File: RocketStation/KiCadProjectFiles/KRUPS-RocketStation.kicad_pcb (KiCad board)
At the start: 4 copper layers, 85 x 56 mm, 46 parts, among them J1 XT30U-M, J2 USB_C_Receptacle_USB2.0_16P, J3 RPi5_Header, J4 B2P-VH-FB-B, J5 B2P-VH-FB-B, J6 B2P-VH-FB-B, U1 PKU5511ESI, U2 AZ1117-3.3, U3 BME280, U4 SP3232, U5 ESP32-S3-WROOM-2, U6 BNO086, U7 E22-900M33S

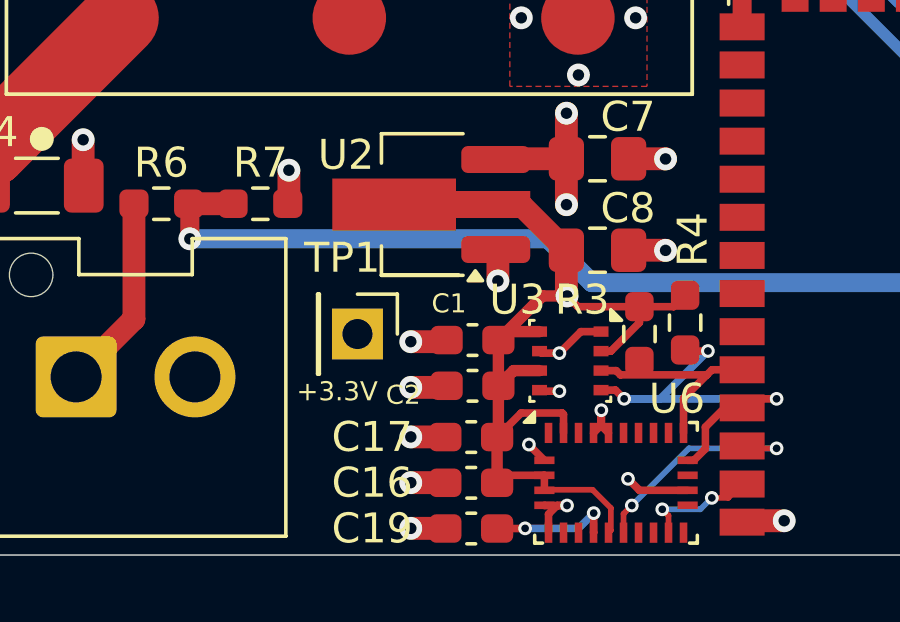
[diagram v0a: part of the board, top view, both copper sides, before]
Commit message: Small fixes for RocketStation v1
Modified RocketStation readme, fixed unconnected 3.3V test point, slightly changed async nets on schematic
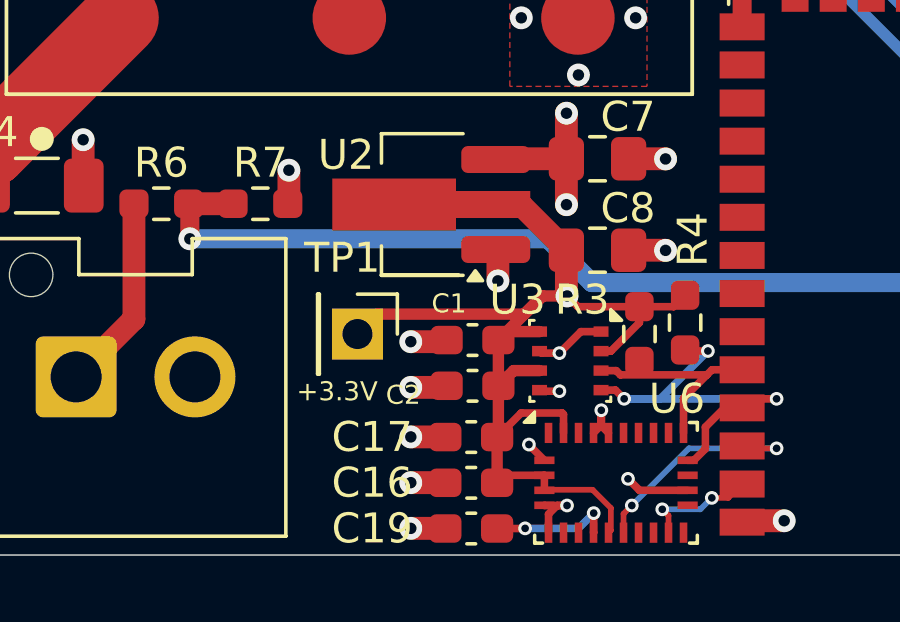
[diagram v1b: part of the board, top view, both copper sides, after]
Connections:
- J4 pad 2: /ASYNC_1 -> /ASYNC_2
- J6 pad 2: /ASYNC_2 -> /ASYNC_1
- U4 pad 14: /ASYNC_1 -> /ASYNC_2
- U4 pad 7: /ASYNC_2 -> /ASYNC_1
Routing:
- net /ASYNC_2: track 24.8 -> 7.64 mm
- net /ASYNC_1: track 7.64 -> 24.8 mm
- net +3V3: track 105.1 -> 111.8 mm
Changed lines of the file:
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@@
 			(layers "*.Cu" "*.Mask")
 			(remove_unused_layers no)
-			(net 52 "/ASYNC_2")
+			(net 51 "/ASYNC_1")
 			(pinfunction "Pin_2")
 			(pintype "passive")
@@
 			(layers "F.Cu" "F.Paste" "F.Mask")
 			(roundrect_rratio 0.25)
-			(net 52 "/ASYNC_2")
+			(net 51 "/ASYNC_1")
 			(pinfunction "T2OUT")
 			(pintype "output")
@@
 			(layers "F.Cu" "F.Paste" "F.Mask")
 			(roundrect_rratio 0.25)
-			(net 51 "/ASYNC_1")
+			(net 52 "/ASYNC_2")
 			(pinfunction "T1OUT")
 			(pintype "output")
@@
 			(layers "*.Cu" "*.Mask")
 			(remove_unused_layers no)
-			(net 51 "/ASYNC_1")
+			(net 52 "/ASYNC_2")
 			(pinfunction "Pin_2")
 			(pintype "passive")
@@
 	)
 	(segment
+		(start 84.5025 70.0695)
+		(end 83.838 70.734)
+		(width 0.381)
+		(layer "F.Cu")
+		(net 1)
+	)
+	(segment
+		(start 89.401 70.0695)
+		(end 84.5025 70.0695)
+		(width 0.381)
+		(layer "F.Cu")
+		(net 1)
+	)
+	(segment
 		(start 92.28375 76.533914)
 		(end 91.674986 75.92515)
@@
 	)
 	(segment
+		(start 90.0065 69.464)
+		(end 89.401 70.0695)
+		(width 0.381)
+		(layer "F.Cu")
+		(net 1)
+	)
+	(segment
 		(start 88.5355 72.459)
 		(end 89.0415 71.953)
@@
 	)
 	(segment
-		(start 99.291 41.4705)
-		(end 102.8045 44.984)
-		(width 0.381)
-		(layer "F.Cu")
-		(net 51)
-	)
-	(segment
-		(start 99.291 38.7985)
-		(end 99.291 41.4705)
-		(width 0.381)
-		(layer "F.Cu")
-		(net 51)
-	)
-	(segment
 		(start 95.014 30.729)
 		(end 95.776 29.967)
 		(width 0.381)
 		(layer "F.Cu")
-		(net 52)
+		(net 51)
 	)
 	(segment
@@
 		(width 0.381)
 		(layer "F.Cu")
-		(net 52)
+		(net 51)
 	)
 	(segment
@@
 		(width 0.381)
 		(layer "F.Cu")
-		(net 52)
+		(net 51)
 	)
 	(segment
@@
 		(width 0.381)
 		(layer "F.Cu")
-		(net 52)
+		(net 51)
 	)
 	(segment
@@
 		(width 0.381)
 		(layer "F.Cu")
-		(net 52)
+		(net 51)
 	)
 	(segment
@@
 		(width 0.381)
 		(layer "F.Cu")
-		(net 52)
+		(net 51)
 	)
 	(segment
@@
 		(width 0.381)
 		(layer "F.Cu")
-		(net 52)
+		(net 51)
 	)
 	(segment
@@
 		(width 0.381)
 		(layer "F.Cu")
-		(net 52)
+		(net 51)
 	)
 	(segment
@@
 		(width 0.381)
 		(layer "F.Cu")
-		(net 52)
+		(net 51)
 	)
 	(segment
@@
 		(width 0.381)
 		(layer "F.Cu")
+		(net 51)
+	)
+	(segment
+		(start 99.291 41.4705)
+		(end 102.8045 44.984)
+		(width 0.381)
+		(layer "F.Cu")
+		(net 52)
+	)
+	(segment
+		(start 99.291 38.7985)
+		(end 99.291 41.4705)
+		(width 0.381)
+		(layer "F.Cu")

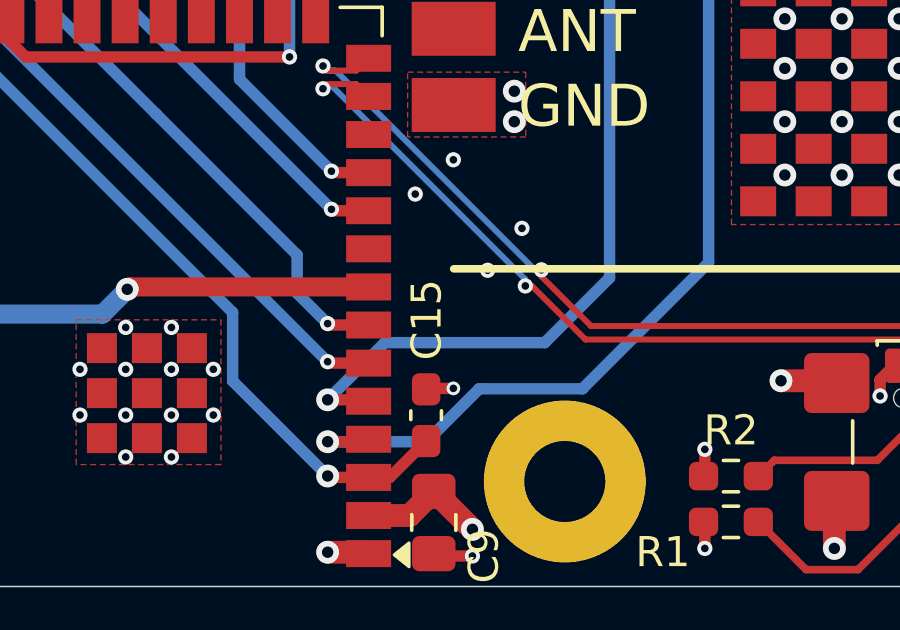
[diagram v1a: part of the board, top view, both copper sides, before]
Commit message: Added optional support for the LR62XE 1W radio
- Created a breakout/adapter board for the LR62XE 1W LoRa radio
- Modified the FemtoSat and RocketStation so that they'll be compatible with the adapter board
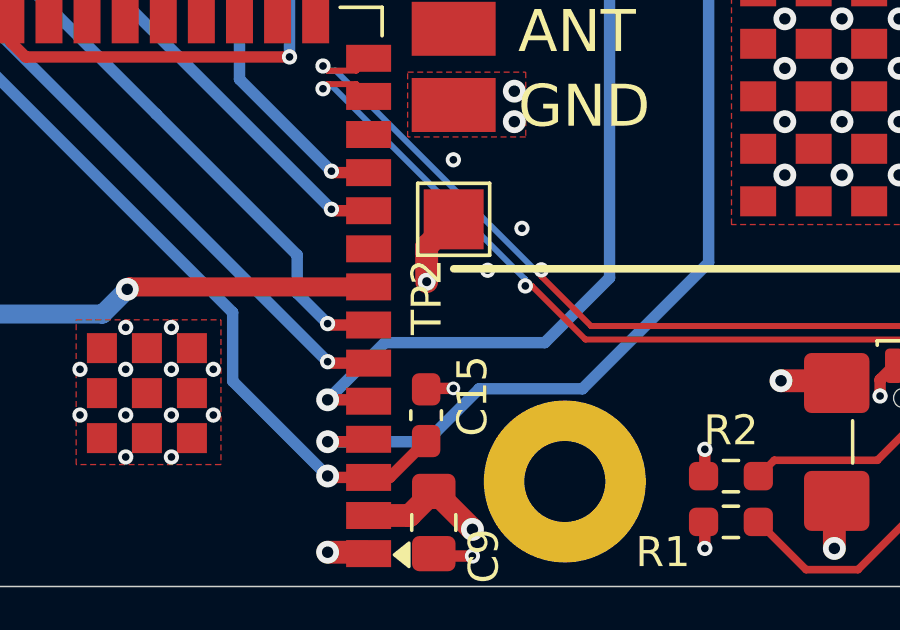
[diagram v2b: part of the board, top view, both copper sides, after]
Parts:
- added TP2: TestPoint, TestPoint:TestPoint_Pad_2.0x2.0mm, F.Cu at (117.0, 65.9)
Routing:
- net +3V3: track 111.8 -> 122.4 mm, vias 4 -> 5
- net GND: track 80.6 -> 80.1 mm, vias 117 -> 116
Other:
- board text added: "KRUPS BaseStation/RocketStation Rev: V2 Serial Number: 12-05-2024"
- board text removed: "KRUPS BaseStation/RocketStation Rev: V1 Serial Number: 11-17-2024"
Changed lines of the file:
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@@
 	(paper "A5")
 	(title_block
-		(date "2024-11-17")
-		(rev "V1")
+		(date "2024-12-05")
+		(rev "V2")
 	)
 	(layers
@@
 		)
 	)
+	(footprint "TestPoint:TestPoint_Pad_2.0x2.0mm"
+		(layer "F.Cu")
+		(at 116.995 65.86)
+		(descr "SMD rectangular pad as test Point, square 2.0mm side length")
+		(tags "test point SMD pad rectangle square")
+		(property "Reference" "TP2"
+			(at -0.899 2.588 90)
+			(layer "F.SilkS")
+			(effects
+				(font
+					(size 1 1)
+					(thickness 0.15)
+				)
+			)
+		)
+		(property "Value" "TestPoint"
+			(at 0 2.05 0)
+			(layer "F.Fab")
+			(effects
+				(font
+					(size 1 1)
+					(thickness 0.15)
+				)
+			)
+		)
+		(property "Footprint" "TestPoint:TestPoint_Pad_2.0x2.0mm"
+			(at 0 0 0)
+			(unlocked yes)
+			(layer "F.Fab")
+			(hide yes)
+			(effects
+				(font
+					(size 1.27 1.27)
+					(thickness 0.15)
+				)
+			)
+		)
+		(property "Datasheet" ""
+			(at 0 0 0)
+			(unlocked yes)
+			(layer "F.Fab")
+			(hide yes)
+			(effects
+				(font
+					(size 1.27 1.27)
+					(thickness 0.15)
+				)
+			)
+		)
+		(property "Description" "test point"
+			(at 0 0 0)
+			(unlocked yes)
+			(layer "F.Fab")
+			(hide yes)
+			(effects
+				(font
+					(size 1.27 1.27)
+					(thickness 0.15)
+				)
+			)
+		)
+		(property ki_fp_filters "Pin* Test*")
+		(sheetname "Root")
+		(sheetfile "KRUPS-RocketStation.kicad_sch")
+		(attr exclude_from_pos_files exclude_from_bom)
+		(fp_line
+			(start -1.2 -1.2)
+			(end 1.2 -1.2)
+			(stroke
+				(width 0.12)
+				(type solid)
+			)
+			(layer "F.SilkS")
+		)
+		(fp_line
+			(start -1.2 1.2)
+			(end -1.2 -1.2)
+			(stroke
+				(width 0.12)
+				(type solid)
+			)
+			(layer "F.SilkS")
+		)
+		(fp_line
+			(start 1.2 -1.2)
+			(end 1.2 1.2)
+			(stroke
+				(width 0.12)
+				(type solid)
+			)
+			(layer "F.SilkS")
+		)
+		(fp_line
+			(start 1.2 1.2)
+			(end -1.2 1.2)
+			(stroke
+				(width 0.12)
+				(type solid)
+			)
+			(layer "F.SilkS")
+		)
+		(fp_line
+			(start -1.5 -1.5)
+			(end -1.5 1.5)
+			(stroke
+				(width 0.05)
+				(type solid)
+			)
+			(layer "F.CrtYd")
+		)
+		(fp_line
+			(start -1.5 -1.5)
+			(end 1.5 -1.5)
+			(stroke
+				(width 0.05)
+				(type solid)
+			)
+			(layer "F.CrtYd")
+		)
+		(fp_line
+			(start 1.5 1.5)
+			(end -1.5 1.5)
+			(stroke
+				(width 0.05)
+				(type solid)
+			)
+			(layer "F.CrtYd")
+		)
+		(fp_line
+			(start 1.5 1.5)
+			(end 1.5 -1.5)
+			(stroke
+				(width 0.05)
+				(type solid)
+			)
+			(layer "F.CrtYd")
+		)
+		(fp_text user "${REFERENCE}"
+			(at 0 -2 0)
+			(layer "F.Fab")
+			(effects
+				(font
+					(size 1 1)
+					(thickness 0.15)
+				)
+			)
+		)
+		(pad "1" smd rect
+			(at 0 0)
+			(size 2 2)
+			(layers "F.Cu" "F.Mask")
+			(net 1 "+3V3")
+			(pinfunction "1")
+			(pintype "passive")
+		)
+	)
 	(footprint "KRUPS-RocketStation:JST_VH_B2P-VH-FB-B_1x02_P3.96mm_Vertical"
 		(layer "F.Cu")
@@
 		(tags "capacitor handsolder")
 		(property "Reference" "C15"
-			(at 3.18 0.018 90)
+			(at 0.64 1.542 90)
 			(layer "F.SilkS")
 			(effects
@@
 		)
 	)
-	(gr_text "KRUPS BaseStation/RocketStation\nRev: V1\nSerial Number:\n11-17-2024"
+	(gr_text "KRUPS BaseStation/RocketStation\nRev: V2\nSerial Number:\n12-05-2024"
 		(at 143.02 73.02 0)
 		(layer "B.SilkS")
@@
 		)
 		(height -12.644)
-		(gr_text "49.0000 mm"
+		(gr_text "1929.1339 mils"
 			(at 48.906 50.1 90)
 			(layer "Cmts.User")
@@
 		)
 		(height -11.718)
-		(gr_text "56.0000 mm"
+		(gr_text "2204.7244 mils"
 			(at 151.268 50.1 90)
 			(layer "Cmts.User")
@@
 		)
 		(height 1.94)
-		(gr_text "6.0000 mm"
+		(gr_text "236.2205 mils"
 			(at 118 83 90)
 			(layer "Cmts.User")
@@
 		)
 		(height -6.428)
-		(gr_text "85.0000 mm"
+		(gr_text "3346.4567 mils"
 			(at 101.7 18.022 0)
 			(layer "Cmts.User")
@@
 		)
 		(height 15.945999)
-		(gr_text "58.0000 mm"
+		(gr_text "2283.4646 mils"
 			(at 91.7 89.395999 0)
 			(layer "Cmts.User")
@@
 		)
 		(height 3.003999)
-		(gr_text "18.0000 mm"
+		(gr_text "708.6614 mils"
 			(at 105.41 86.347999 0)
 			(layer "Cmts.User")
@@
 	)
 	(segment
+		(start 116.096 67.94)
+		(end 116.096 66.759)
+		(width 0.762)
+		(layer "F.Cu")
+		(net 1)
+	)
+	(segment
 		(start 88.7425 75.442)
 		(end 88.4925 75.692)
@@
 	)
 	(segment
+		(start 116.096 66.759)
+		(end 116.995 65.86)
+		(width 0.762)
+		(layer "F.Cu")
+		(net 1)
+	)
+	(segment
 		(start 90.706 73.411)
 		(end 90.66 73.365)
@@
 	)
 	(via
+		(at 116.096 67.94)
+		(size 0.6)
+		(drill 0.3)
+		(layers "F.Cu" "B.Cu")
+		(net 1)
+	)
+	(via
 		(at 101.999 40)
 		(size 0.762)
@@
 	)
 	(segment
+		(start 115.588 75.941)
+		(end 117.366 75.941)
+		(width 0.762)
+		(layer "In2.Cu")
+		(net 1)
+	)
+	(segment
 		(start 96.919 40)
 		(end 101.999 40)
@@
 	)
 	(segment
+		(start 97.3 75.941)
+		(end 115.588 75.941)
+		(width 0.762)
+		(layer "In2.Cu")
+		(net 1)
+	)
+	(segment
 		(start 95.9355 40.9835)
 		(end 96.919 40)
@@
 	)
 	(segment
-		(start 97.3 75.941)
-		(end 117.366 75.941)
+		(start 115.588 75.941)
+		(end 116.096 75.433)
+		(width 0.762)
+		(layer "In2.Cu")
+		(net 1)
+	)
+	(segment
+		(start 116.096 75.433)
+		(end 116.096 67.94)
 		(width 0.762)
 		(layer "In2.Cu")
@@
 	)
 	(via
-		(at 115.715 65.019)
-		(size 0.508)
-		(drill 0.254)
-		(layers "F.Cu" "B.Cu")
-		(free yes)
-		(net 2)
-	)
-	(via
 		(at 138.956 59.939)
 		(size 0.762)
@@
 		(width 0.381)
 		(layer "In2.Cu")
-		(net 2)
-	)
-	(segment
-		(start 115.715 65.019)
-		(end 116.096 64.638)
-		(width 0.381)
-		(layer "In2.Cu")

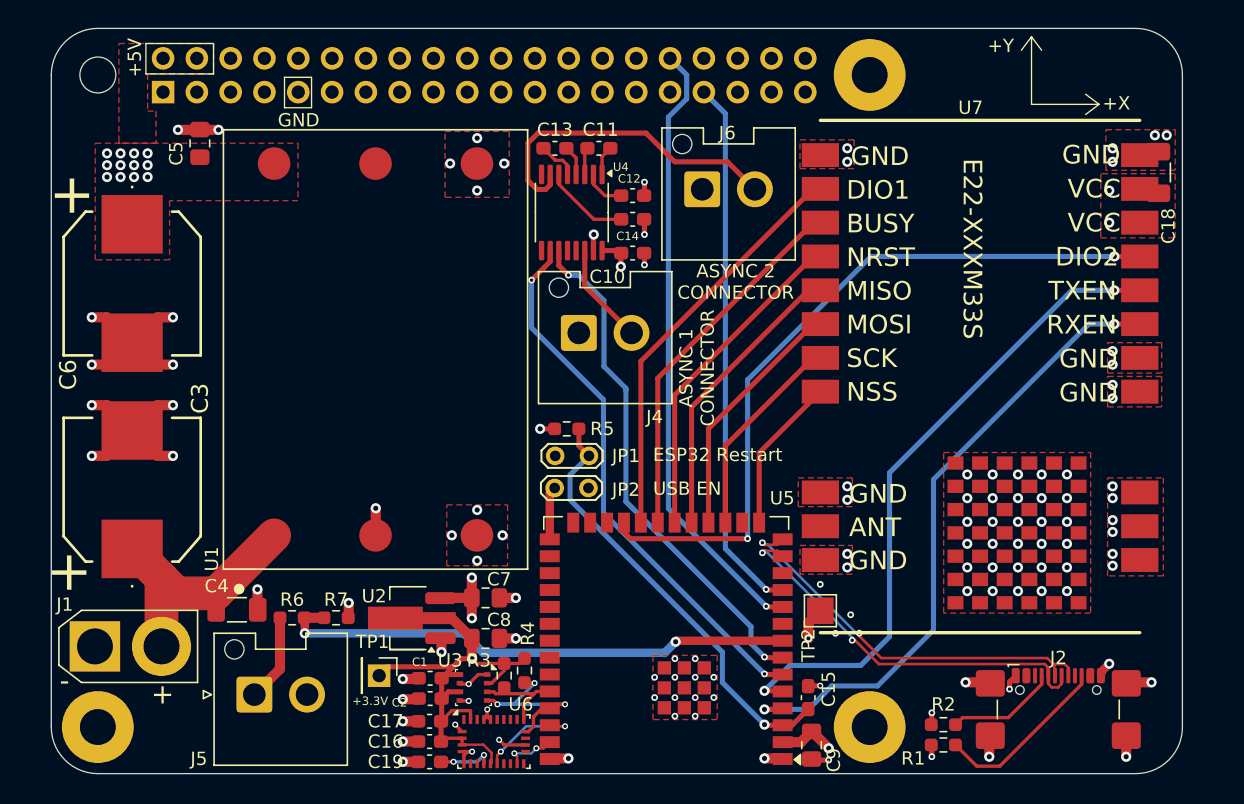
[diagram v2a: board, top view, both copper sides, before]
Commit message: Design Review Updates
Large number of design changes to both the FemtoSat (V5) and RocketStation (V3)

On both boards:
- Swapped the ESP32-S3-WROOM-2 modules to WROOM-1 modules due to supply issues
- Swapped power connectors to JST VH, data connectors to JST GH
- Added "Space Systems Lab, University of Kentucky, Lexington KY, USA, Earth" to the silkscreens
- Added test pads for IO pins, I2C bus, power
- Added LEDs connected to IO pins
- Changed power indication LEDs to a brighter LED
- Reformatted BOMs, they can now be generated by KiCad rather than being made by hand
- Updated documentation, 3D models

For Femtosat
- Removed 1 enclosure switch & MOSFET
- Moved a screw hole

and a bunch of other minor changes that I've forgotten
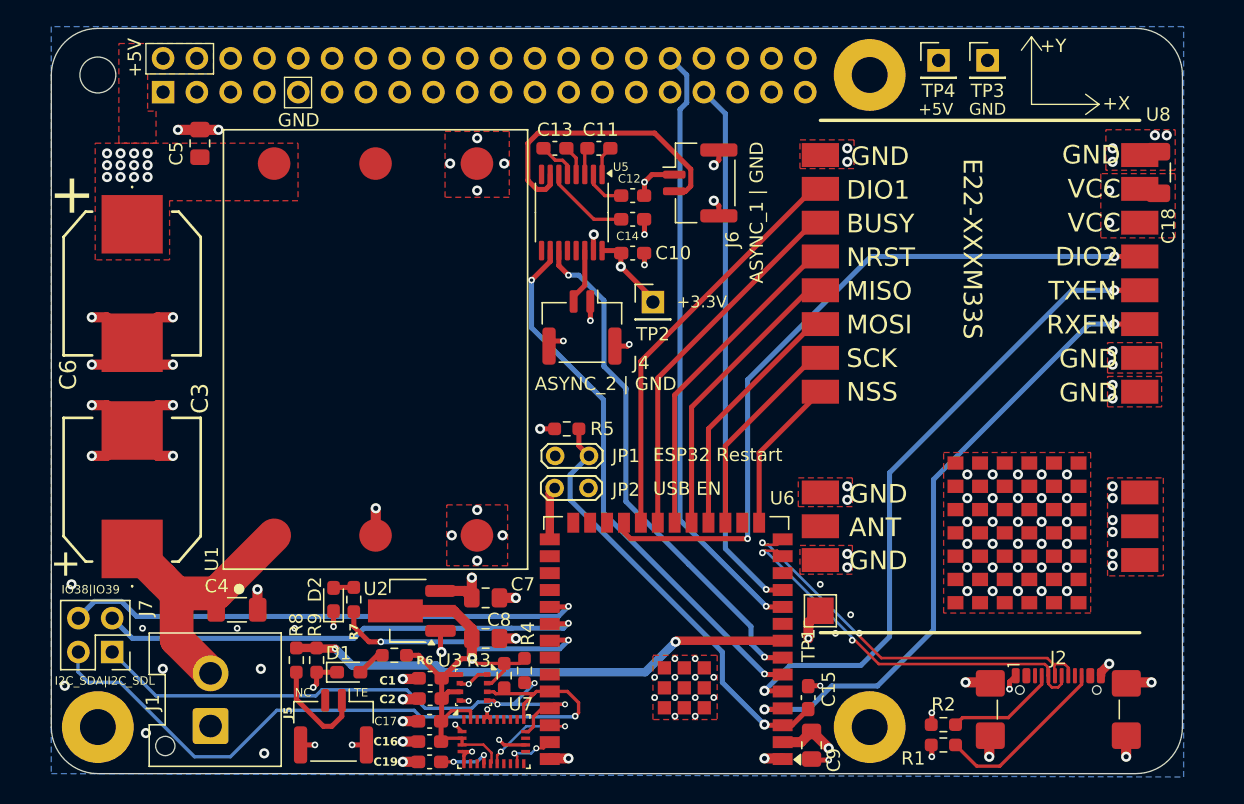
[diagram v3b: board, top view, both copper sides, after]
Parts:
- removed the TP1 at (83.8, 70.7)
- added D1: LED, Diode_SMD:D_0603_1608Metric_Pad1.05x0.95mm_HandSolder, F.Cu at (81.6, 70.5)
- added D2: LED, Diode_SMD:D_0603_1608Metric_Pad1.05x0.95mm_HandSolder, F.Cu at (80.4, 65.0)
- added J7: Conn_02x02, Connector_PinHeader_2.54mm:PinHeader_2x02_P2.54mm_Vertical, F.Cu at (63.8, 69.0)
- added R6: 68, Resistor_SMD:R_0603_1608Metric_Pad0.98x0.95mm_HandSolder, F.Cu at (85.0, 69.2)
- added R7: 68, Resistor_SMD:R_0603_1608Metric_Pad0.98x0.95mm_HandSolder, F.Cu at (81.9, 65.0)
- added TP2: TestPoint, Connector_PinHeader_2.54mm:PinHeader_1x01_P2.54mm_Vertical, F.Cu at (104.4, 42.7)
- added TP3: TestPoint, Connector_PinHeader_2.54mm:PinHeader_1x01_P2.54mm_Vertical, F.Cu at (129.6, 24.5)
- added TP4: TestPoint, Connector_PinHeader_2.54mm:PinHeader_1x01_P2.54mm_Vertical, F.Cu at (125.9, 24.5)
- J1: value XT30U-M -> B2P-VH-FB-B; footprint Connector_AMASS:AMASS_XT30U-M_1x02_P5.0mm_Vertical -> Connector_JST:JST_VH_B2P-VH-FB-B_1x02_P3.96mm_Vertical
- J4, J5, J6: value B2P-VH-FB-B -> BM02B-GHS-TBT; footprint KRUPS-RocketStation:JST_VH_B2P-VH-FB-B_1x02_P3.96mm_Vertical -> Connector_JST:JST_GH_BM02B-GHS-TBT_1x02-1MP_P1.25mm_Vertical
- moved J1 10.5 mm to (71.2, 74.5), turned to 90 degrees
- moved J5 6.41 mm to (80.4, 74.5), turned to 180 degrees
- moved R9 3.50 mm to (79.1, 69.6), turned to 90 degrees
- moved R8 3.19 mm to (77.6, 69.6), turned to -90 degrees
- moved U2 0.55 mm to (86.0, 65.9)
- moved J6 0.50 mm to (108.0, 33.7), turned to -90 degrees
- moved J4 0.47 mm to (99.1, 44.6), turned to 180 degrees
- renumbered R6 to R8, R7 to R9, TP2 to TP1, U4 to U5, U5 to U6, U6 to U7, U7 to U8
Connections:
- U6 pad 31: unconnected-(U5-IO38-Pad31) -> /IO38
- U6 pad 32: unconnected-(U5-MTCK/IO39-Pad32) -> /IO39
- U6 pad 33: unconnected-(U5-MTDO/IO40-Pad33) -> /IO40
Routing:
- net /I2C_SDA: track 7.09 -> 53.9 mm, vias 0 -> 1
- net /IO38: track 0.00 -> 39.6 mm, vias 0 -> 1
- net /IO39: track 0.00 -> 36.8 mm, vias 0 -> 1
- net /I2C_SCL: track 14.4 -> 45.8 mm
- net /IO40: track 0.00 -> 19.6 mm, vias 0 -> 2
- net GND: track 80.1 -> 93.8 mm, vias 116 -> 133
- net /ASYNC_2: track 7.64 -> 4.17 mm
- net /ASYNC_1: track 24.8 -> 22.0 mm
- net +5V: track 127.1 -> 129.2 mm, vias 16 -> 15
- net Net-(D1-A): track 0.00 -> 2.17 mm
- net Net-(J1-Pin_2): track 19.0 -> 20.9 mm
- net +3V3: track 122.4 -> 124.3 mm
- net Net-(D2-A): track 0.00 -> 1.54 mm
- net /TE_SENSE: track 39.6 -> 38.3 mm
- net Net-(J5-Pin_1): track 6.57 -> 7.80 mm
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- added copper zone on B.Cu, net GND
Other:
- board text added: "+"
- board text added: "+18V TO +75V"
- board text added: "-"
- board text added: "ASYNC_1 | GND"
- board text added: "ASYNC_2 | GND"
- board text added: "All mounting holes are M2.5 The height of the 40 pin GPIO connector can be adjusted during PCB assembly (the length of the connector's leads will be pretty long), so the height shown in the 3D model is not accurate"
- board text added: "I2C_SDA|I2C_SDL"
- board text added: "IO38|IO39"
- board text added: "NC"
- board text added: "Space Systems Lab, University of Kentucky, Lexington KY, USA, Earth KRUPS BaseStation/RocketStation Rev: V3 Serial Number: 12-27-2024"
- board text added: "TE"
- board text removed: "ASYNC 1 CONNECTOR"
- board text removed: "ASYNC 2 CONNECTOR"
- board text removed: "All mounting holes are M2.5 The height of the 40 pin GPIO connector can be adjusted during PCB assembly (the length of the connector's leads will be pretty long), so the height shown in the 3D model is not all that important"
- board text removed: "KRUPS BaseStation/RocketStation Rev: V2 Serial Number: 12-05-2024"
- board text removed: "PIN 1 GND"
- board text removed: "PIN 2 ASYNC 1"
- board text removed: "PIN 2 ASYNC 2"
